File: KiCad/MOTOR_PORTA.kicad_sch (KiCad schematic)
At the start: 0 parts

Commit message: Nova versió diagrama de blocs + BOM actualitzat + Nova versió KiCad
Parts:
- added C15, C18: 100nF, symbol Device:C
- added C16: 10uF, symbol Device:C
- added R1: 1k, Resistor_SMD:R_0805_2012Metric_Pad1.20x1.40mm_HandSolder, symbol Device:R
- added R10, R9: 3.3k, Resistor_SMD:R_0805_2012Metric_Pad1.20x1.40mm_HandSolder, symbol Device:R
- added U7: VNH5019A-E, Package_SO:ST_MultiPowerSO-30, symbol Driver_Motor:VNH5019A-E
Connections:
- new net: R1.1, U7.8 (CS)
- new net: C18.2, U7.11 (CP)
- new net: R10.1, U7.5 (EN/DIAGA)
- new net: R9.1, U7.9 (EN/DIAGB)
- new net DOOR_DIAGA: R10.2
- new net DOOR_DIAGB: R9.2
- new net DOOR_INA: U7.4 (INA)
- new net DOOR_INB: U7.10 (INB)
- new net DOOR_OUTA: U7.1 (OUTA), U7.25 (OUTA), U7.30 (OUTA), U7.33 (OUTA)
- new net DOOR_OUTB: U7.15 (OUTB), U7.16 (OUTB), U7.21 (OUTB), U7.32 (OUTB)
- new net DOOR_PWM: U7.7 (PWM)
- new net GND: C15.2, C16.2, C18.1, R1.2
- new net GND_PWR: U7.18 (GNDB), U7.19 (GNDB), U7.20 (GNDB), U7.26 (GNDA), U7.27 (GNDA), U7.28 (GNDA)
- new net VBAT_PROT: C15.1, C16.1, U7.12 (VBAT), U7.13 (VCC), U7.23 (VCC), U7.3 (VCC), U7.31 (VCC)
- new net VDD_3V3: U7.6 (CS_DIS)

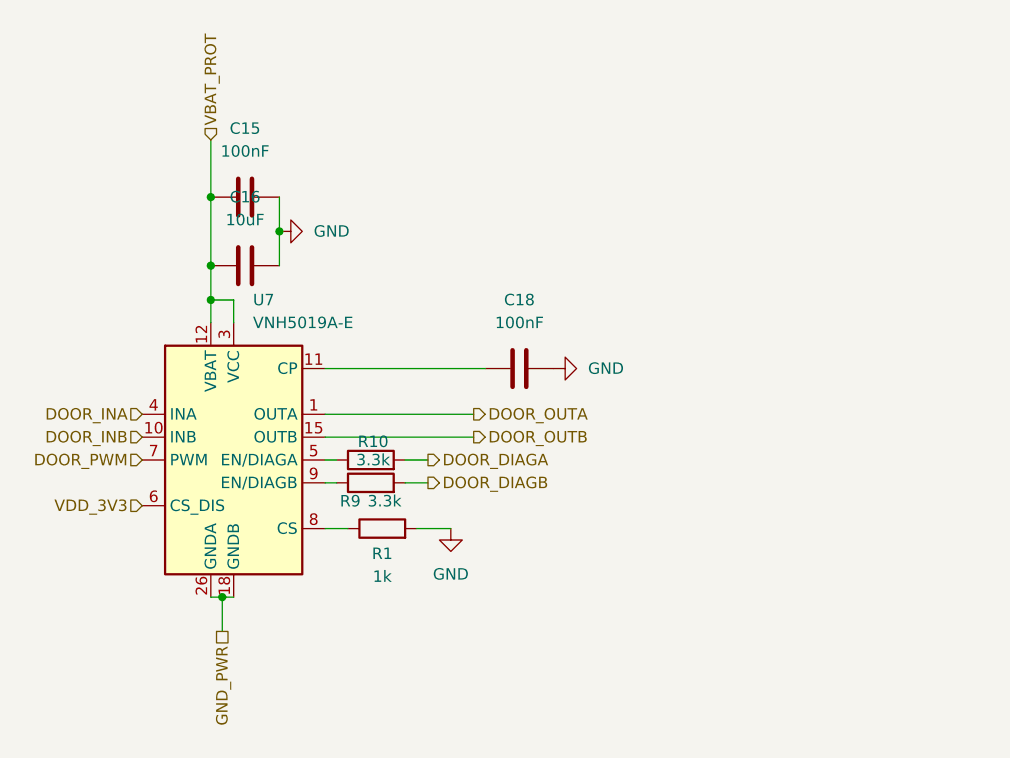
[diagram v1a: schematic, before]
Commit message: Resistències pull-up arreglades als motors
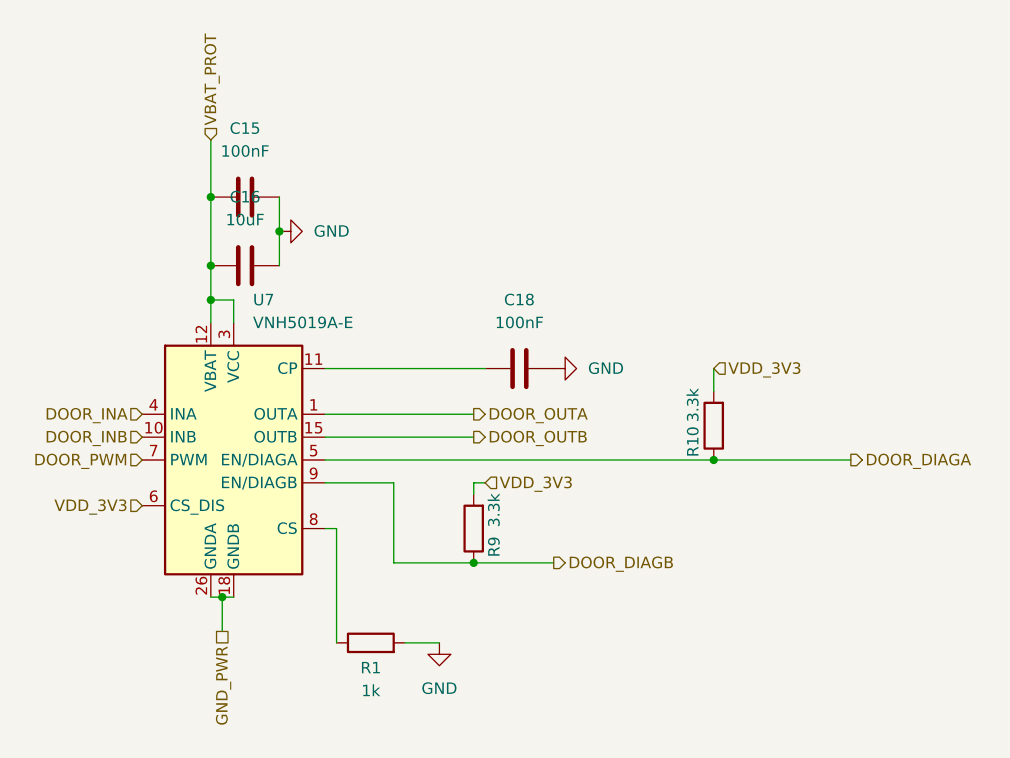
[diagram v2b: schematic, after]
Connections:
- net DOOR_DIAGA: now also R10.1, U7.5 (EN/DIAGA); no longer R10.2
- net DOOR_DIAGB: now also R9.1, U7.9 (EN/DIAGB); no longer R9.2
- net VDD_3V3: now also R10.2, R9.2
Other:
- moved on the sheet: R1

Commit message: Etiquetes de GND i VCC 3.3V canviades a simbols
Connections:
- net GND_PWR renamed GNDPWR
- net VDD_3V3 renamed +3.3V

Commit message: Correció etapa d'alimentació e Inputs
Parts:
- renumbered C15 to C13, C16 to C14, C18 to C15, R1 to R11, R9 to R12, R10 to R13, U7 to U6
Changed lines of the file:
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@@
 		(dnp no)
 		(fields_autoplaced yes)
-		(property "Reference" "#PWR08"
+		(property "Reference" "#PWR039"
 			(at 153.67 73.66 0)
 			(effects
@@
 			(project "PROJECTE_EINES"
 				(path "/347831db-5db9-4aff-ad32-e56fd770e219/839c8b34-4c01-48c7-9037-58d60b295fe6"
-					(reference "#PWR08")
+					(reference "#PWR039")
 					(unit 1)
 				)
@@
 		(on_board yes)
 		(dnp no)
-		(property "Reference" "#PWR040"
+		(property "Reference" "#PWR037"
 			(at 129.54 107.95 0)
 			(effects
@@
 			(project ""
 				(path "/347831db-5db9-4aff-ad32-e56fd770e219/839c8b34-4c01-48c7-9037-58d60b295fe6"
-					(reference "#PWR040")
+					(reference "#PWR037")
 					(unit 1)
 				)
@@
 		(dnp no)
 		(fields_autoplaced yes)
-		(property "Reference" "C16"
+		(property "Reference" "C14"
 			(at 143.51 69.85 90)
 			(effects
@@
 			(project "PROJECTE_EINES"
 				(path "/347831db-5db9-4aff-ad32-e56fd770e219/839c8b34-4c01-48c7-9037-58d60b295fe6"
-					(reference "C16")
+					(reference "C14")
 					(unit 1)
 				)
@@
 		(on_board yes)
 		(dnp no)
-		(property "Reference" "R1"
+		(property "Reference" "R11"
 			(at 157.48 122.174 90)
 			(effects
@@
 			(project ""
 				(path "/347831db-5db9-4aff-ad32-e56fd770e219/839c8b34-4c01-48c7-9037-58d60b295fe6"
-					(reference "R1")
+					(reference "R11")
 					(unit 1)
 				)
@@
 		(on_board yes)
 		(dnp no)
-		(property "Reference" "R9"
+		(property "Reference" "R12"
 			(at 171.196 108.712 90)
 			(effects
@@
 			(project "PROJECTE_EINES"
 				(path "/347831db-5db9-4aff-ad32-e56fd770e219/839c8b34-4c01-48c7-9037-58d60b295fe6"
-					(reference "R9")
+					(reference "R12")
 					(unit 1)
 				)
@@
 		(dnp no)
 		(fields_autoplaced yes)
-		(property "Reference" "#PWR011"
+		(property "Reference" "#PWR040"
 			(at 165.1 125.73 0)
 			(effects
@@
 			(project "PROJECTE_EINES"
 				(path "/347831db-5db9-4aff-ad32-e56fd770e219/839c8b34-4c01-48c7-9037-58d60b295fe6"
-					(reference "#PWR011")
+					(reference "#PWR040")
 					(unit 1)
 				)
@@
 		(on_board yes)
 		(dnp no)
-		(property "Reference" "R10"
+		(property "Reference" "R13"
 			(at 193.294 97.028 90)
 			(effects
@@
 			(project "PROJECTE_EINES"
 				(path "/347831db-5db9-4aff-ad32-e56fd770e219/839c8b34-4c01-48c7-9037-58d60b295fe6"
-					(reference "R10")
+					(reference "R13")
 					(unit 1)
 				)
@@
 		(on_board yes)
 		(dnp no)
-		(property "Reference" "C18"
+		(property "Reference" "C15"
 			(at 173.99 81.28 90)
 			(effects
@@
 			(project "PROJECTE_EINES"
 				(path "/347831db-5db9-4aff-ad32-e56fd770e219/839c8b34-4c01-48c7-9037-58d60b295fe6"
-					(reference "C18")
+					(reference "C15")
 					(unit 1)
 				)
@@
 		(dnp no)
 		(fields_autoplaced yes)
-		(property "Reference" "C15"
+		(property "Reference" "C13"
 			(at 143.51 62.23 90)
 			(effects
@@
 			(project "PROJECTE_EINES"
 				(path "/347831db-5db9-4aff-ad32-e56fd770e219/839c8b34-4c01-48c7-9037-58d60b295fe6"
-					(reference "C15")
+					(reference "C13")
 					(unit 1)
 				)
@@
 		(on_board yes)
 		(dnp no)
-		(property "Reference" "#PWR042"
+		(property "Reference" "#PWR041"
 			(at 168.91 106.68 0)
 			(effects
@@
 			(project "PROJECTE_EINES"
 				(path "/347831db-5db9-4aff-ad32-e56fd770e219/839c8b34-4c01-48c7-9037-58d60b295fe6"
-					(reference "#PWR042")
+					(reference "#PWR041")
 					(unit 1)
 				)
@@
 		(dnp no)
 		(fields_autoplaced yes)
-		(property "Reference" "U7"
+		(property "Reference" "U6"
 			(at 144.3833 81.28 0)
 			(effects
@@
 			(project "PROJECTE_EINES"
 				(path "/347831db-5db9-4aff-ad32-e56fd770e219/839c8b34-4c01-48c7-9037-58d60b295fe6"
-					(reference "U7")
+					(reference "U6")
 					(unit 1)
 				)
@@
 		(dnp no)
 		(fields_autoplaced yes)
-		(property "Reference" "#PWR041"
+		(property "Reference" "#PWR038"
 			(at 140.97 123.19 0)
 			(effects
@@
 			(project ""
 				(path "/347831db-5db9-4aff-ad32-e56fd770e219/839c8b34-4c01-48c7-9037-58d60b295fe6"
-					(reference "#PWR041")
+					(reference "#PWR038")
 					(unit 1)
 				)
@@
 		(dnp no)
 		(fields_autoplaced yes)
-		(property "Reference" "#PWR010"
+		(property "Reference" "#PWR042"
 			(at 184.15 88.9 0)
 			(effects
@@
 			(project "PROJECTE_EINES"
 				(path "/347831db-5db9-4aff-ad32-e56fd770e219/839c8b34-4c01-48c7-9037-58d60b295fe6"
-					(reference "#PWR010")
-					(unit 1)
-				)
+					(reference "#PWR042")
+					(unit 1)
+				)

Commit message: Versió final Esquematic
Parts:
- C_CP_DOOR1: renamed from C15; footprint (none) -> Capacitor_SMD:C_0805_2012Metric
- C_VDD_DOOR1: renamed from C13; footprint (none) -> Capacitor_SMD:C_0805_2012Metric
- C_VDD_DOOR2: renamed from C14; footprint (none) -> Capacitor_SMD:CP_Elec_8x10
- R_CS_DOOR1: renamed from R11; footprint Resistor_SMD:R_0805_2012Metric_Pad1.20x1.40mm_HandSolder -> Resistor_SMD:R_0805_2012Metric
- R_DIAGA_DOOR1: renamed from R13; footprint Resistor_SMD:R_0805_2012Metric_Pad1.20x1.40mm_HandSolder -> Resistor_SMD:R_0805_2012Metric
- R_DIAGB_DOOR1: renamed from R12; footprint Resistor_SMD:R_0805_2012Metric_Pad1.20x1.40mm_HandSolder -> Resistor_SMD:R_0805_2012Metric
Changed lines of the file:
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@@
 		(on_board yes)
 		(dnp no)
-		(fields_autoplaced yes)
-		(property "Reference" "C14"
-			(at 143.51 69.85 90)
+		(property "Reference" "C_VDD_DOOR2"
+			(at 151.638 78.74 90)
 			(effects
 				(font
@@
 		)
 		(property "Value" "10uF"
-			(at 143.51 72.39 90)
-			(effects
-				(font
-					(size 1.27 1.27)
-				)
-			)
-		)
-		(property "Footprint" ""
+			(at 143.51 74.422 90)
+			(effects
+				(font
+					(size 1.27 1.27)
+				)
+			)
+		)
+		(property "Footprint" "Capacitor_SMD:CP_Elec_8x10"
 			(at 147.32 76.5048 0)
 			(effects
@@
 			(project "PROJECTE_EINES"
 				(path "/347831db-5db9-4aff-ad32-e56fd770e219/839c8b34-4c01-48c7-9037-58d60b295fe6"
-					(reference "C14")
+					(reference "C_VDD_DOOR2")
 					(unit 1)
 				)
@@
 		(on_board yes)
 		(dnp no)
-		(property "Reference" "R11"
+		(property "Reference" "R_CS_DOOR1"
 			(at 157.48 122.174 90)
 			(effects
@@
 			)
 		)
-		(property "Footprint" "Resistor_SMD:R_0805_2012Metric_Pad1.20x1.40mm_HandSolder"
+		(property "Footprint" "Resistor_SMD:R_0805_2012Metric"
 			(at 157.48 121.158 90)
 			(effects
@@
 			(project ""
 				(path "/347831db-5db9-4aff-ad32-e56fd770e219/839c8b34-4c01-48c7-9037-58d60b295fe6"
-					(reference "R11")
+					(reference "R_CS_DOOR1")
 					(unit 1)
 				)
@@
 		(on_board yes)
 		(dnp no)
-		(property "Reference" "R12"
-			(at 171.196 108.712 90)
+		(property "Reference" "R_DIAGB_DOOR1"
+			(at 174.244 107.188 90)
 			(effects
 				(font
@@
 		)
 		(property "Value" "3.3k"
-			(at 171.196 104.648 90)
-			(effects
-				(font
-					(size 1.27 1.27)
-				)
-			)
-		)
-		(property "Footprint" "Resistor_SMD:R_0805_2012Metric_Pad1.20x1.40mm_HandSolder"
+			(at 171.958 107.188 90)
+			(effects
+				(font
+					(size 1.27 1.27)
+				)
+			)
+		)
+		(property "Footprint" "Resistor_SMD:R_0805_2012Metric"
 			(at 170.688 106.68 90)
 			(effects
@@
 			(project "PROJECTE_EINES"
 				(path "/347831db-5db9-4aff-ad32-e56fd770e219/839c8b34-4c01-48c7-9037-58d60b295fe6"
-					(reference "R12")
+					(reference "R_DIAGB_DOOR1")
 					(unit 1)
 				)
@@
 		(on_board yes)
 		(dnp no)
-		(property "Reference" "R13"
-			(at 193.294 97.028 90)
+		(property "Reference" "R_DIAGA_DOOR1"
+			(at 193.04 95.758 90)
 			(effects
 				(font
@@
 		)
 		(property "Value" "3.3k"
-			(at 193.294 92.964 90)
-			(effects
-				(font
-					(size 1.27 1.27)
-				)
-			)
-		)
-		(property "Footprint" "Resistor_SMD:R_0805_2012Metric_Pad1.20x1.40mm_HandSolder"
+			(at 199.39 96.012 90)
+			(effects
+				(font
+					(size 1.27 1.27)
+				)
+			)
+		)
+		(property "Footprint" "Resistor_SMD:R_0805_2012Metric"
 			(at 197.358 95.25 90)
 			(effects
@@
 			(project "PROJECTE_EINES"
 				(path "/347831db-5db9-4aff-ad32-e56fd770e219/839c8b34-4c01-48c7-9037-58d60b295fe6"
-					(reference "R13")
+					(reference "R_DIAGA_DOOR1")
 					(unit 1)
 				)
@@
 		(on_board yes)
 		(dnp no)
-		(property "Reference" "C15"
+		(property "Reference" "C_CP_DOOR1"
 			(at 173.99 81.28 90)
 			(effects
@@
 			)
 		)
-		(property "Footprint" ""
+		(property "Footprint" "Capacitor_SMD:C_0805_2012Metric"
 			(at 170.18 89.8652 0)
 			(effects
@@
 			(project "PROJECTE_EINES"
 				(path "/347831db-5db9-4aff-ad32-e56fd770e219/839c8b34-4c01-48c7-9037-58d60b295fe6"
-					(reference "C15")
+					(reference "C_CP_DOOR1")
 					(unit 1)
 				)
@@
 		(on_board yes)
 		(dnp no)
-		(fields_autoplaced yes)
-		(property "Reference" "C13"
-			(at 143.51 62.23 90)
+		(property "Reference" "C_VDD_DOOR1"
+			(at 150.114 64.262 90)
 			(effects
 				(font
@@
 		)
 		(property "Value" "100nF"
-			(at 143.51 64.77 90)
-			(effects
-				(font
-					(size 1.27 1.27)
-				)
-			)
-		)
-		(property "Footprint" ""
+			(at 143.764 66.802 90)
+			(effects
+				(font
+					(size 1.27 1.27)
+				)
+			)
+		)
+		(property "Footprint" "Capacitor_SMD:C_0805_2012Metric"
 			(at 147.32 68.8848 0)
 			(effects
@@
 			(project "PROJECTE_EINES"
 				(path "/347831db-5db9-4aff-ad32-e56fd770e219/839c8b34-4c01-48c7-9037-58d60b295fe6"
-					(reference "C13")
-					(unit 1)
-				)
+					(reference "C_VDD_DOOR1")
+					(unit 1)
+				)
